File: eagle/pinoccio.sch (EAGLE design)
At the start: 59 parts, among them IC1 ATMEGA16U2QFN32, J1 AVR_SPI_PRG_6, Q1 16MHz, Q2 32.768k, Q3 16MHz, U1 MCP73831, U2 TPS78233, U4 ATMEGA128RFA1, X1 USB-MICROB, Y2 ANTENNA2SMD5

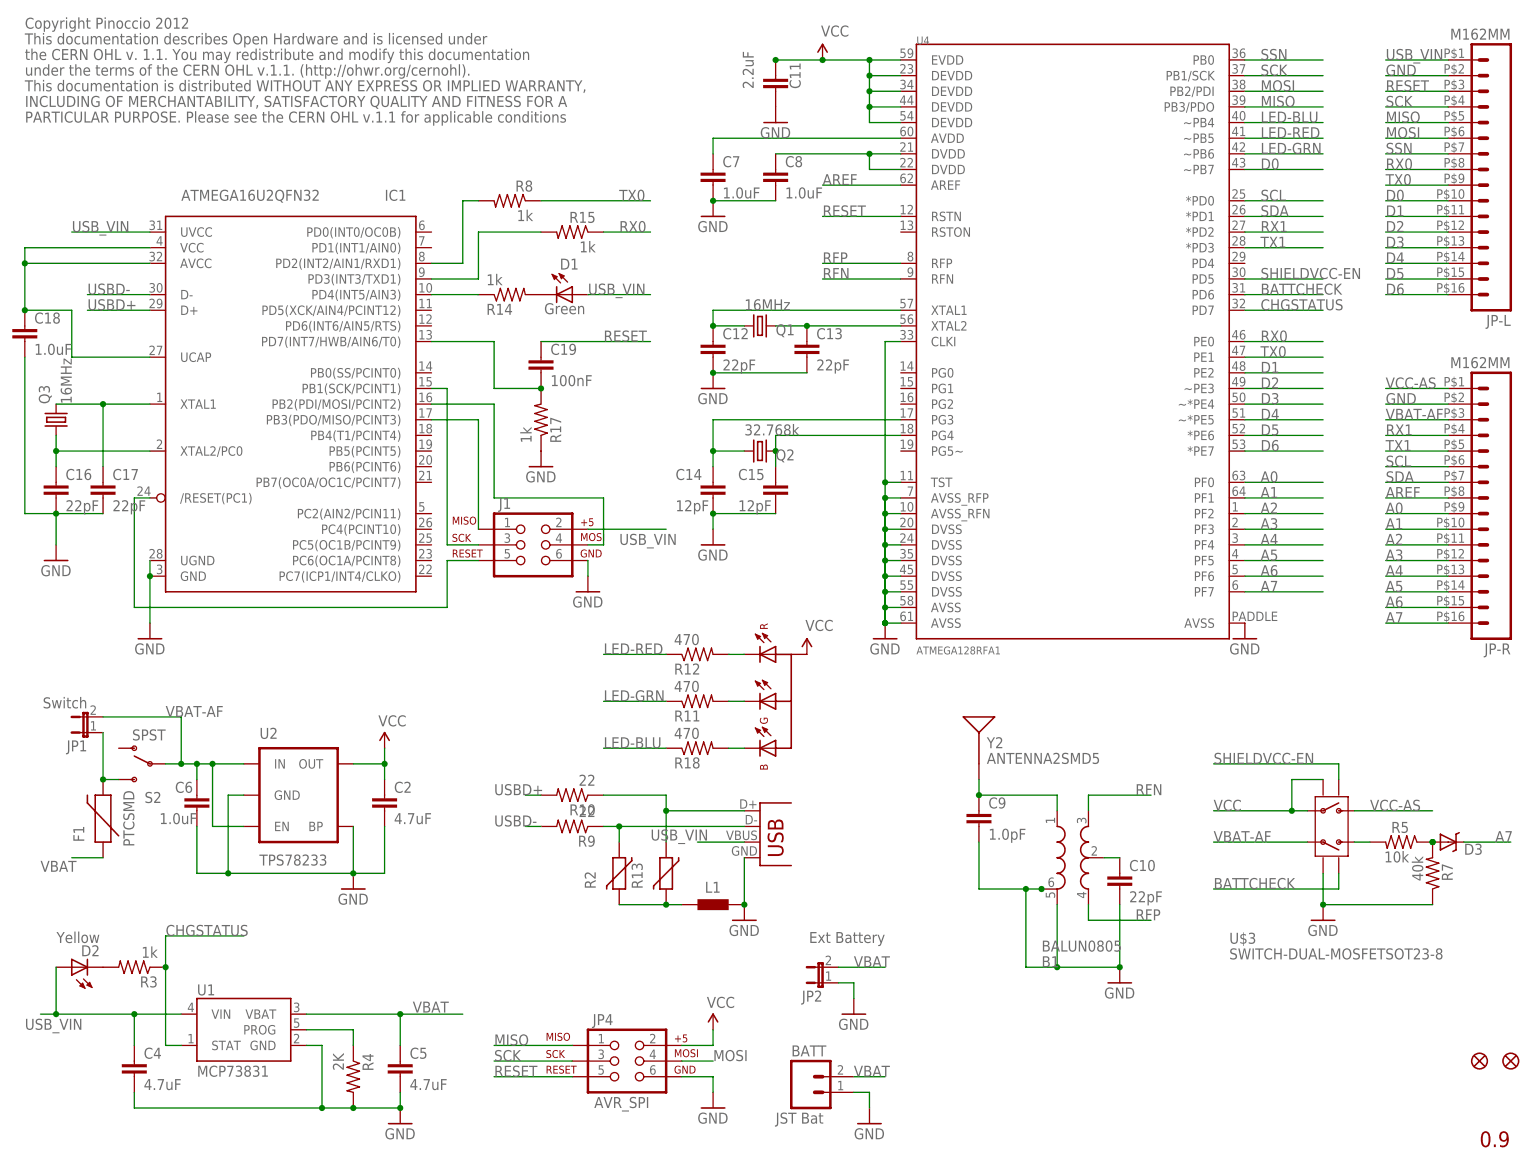
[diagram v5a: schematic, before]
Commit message: Fix changes needed for reset pullup resistor for 16U2
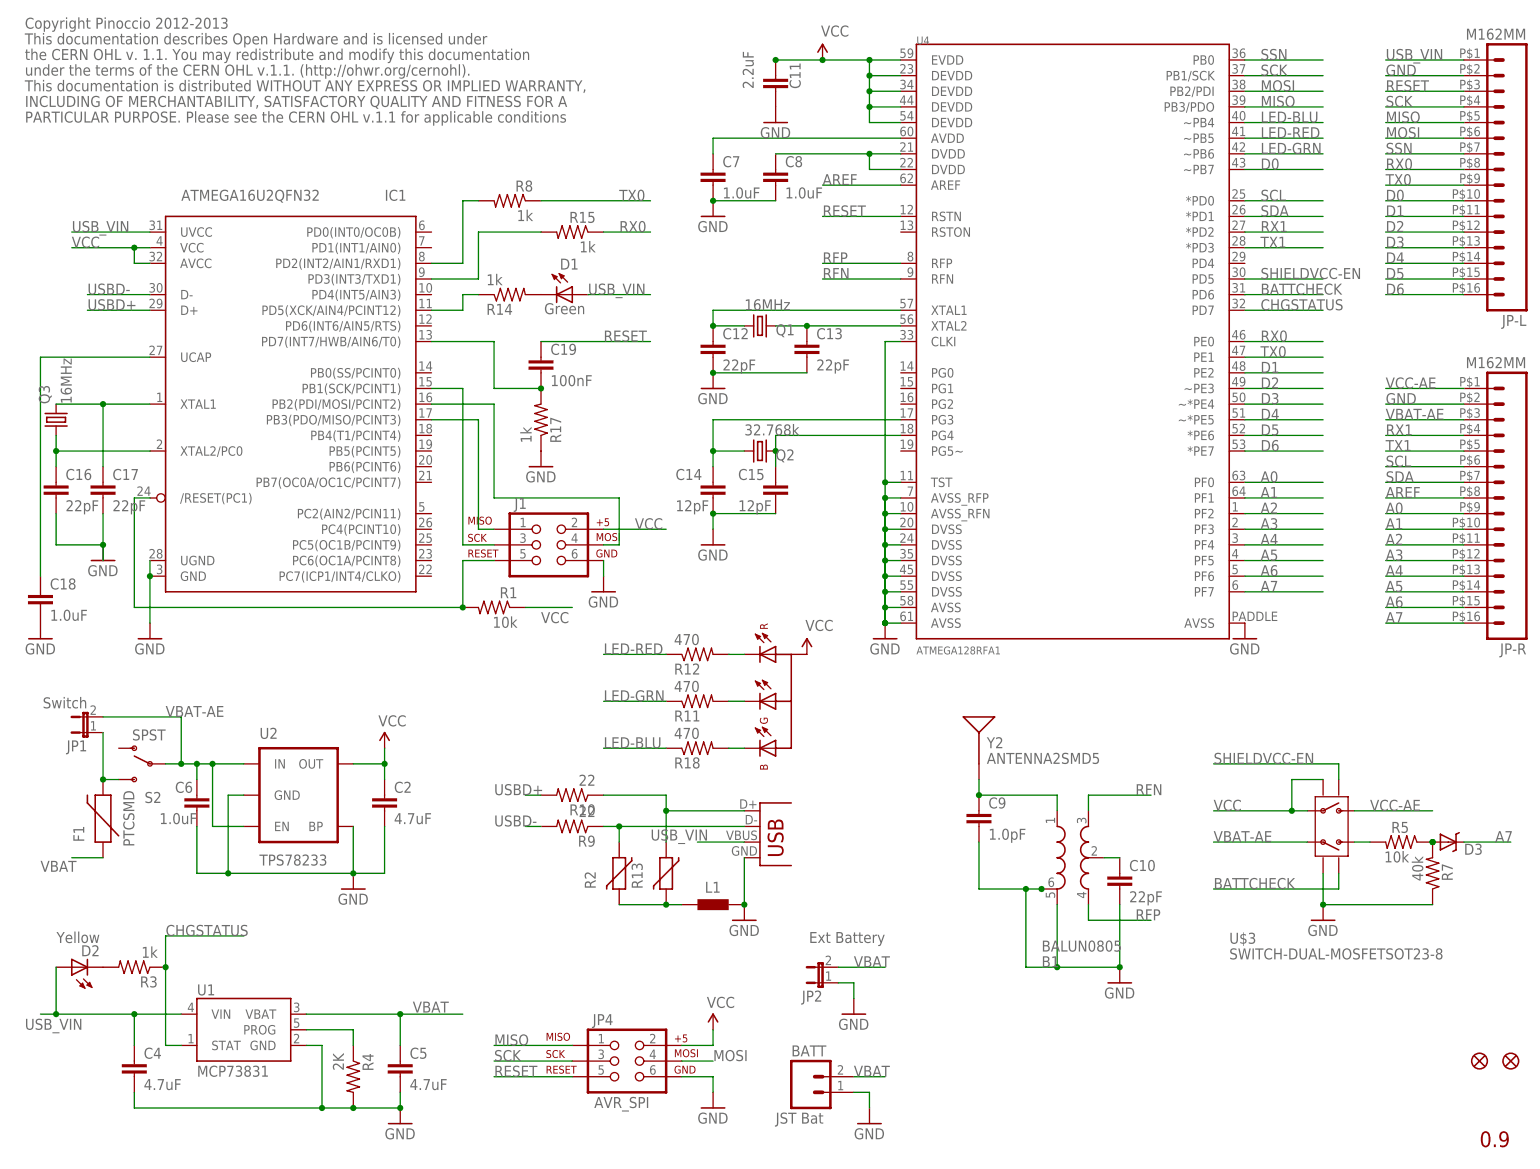
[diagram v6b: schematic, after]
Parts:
- added R1: 10k, Pinoccio:RESISTOR0402-RES
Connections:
- net VBAT-AF renamed VBAT-AE
- net VCC-AS renamed VCC-AE
- removed net N$23: C18.1, IC1.AVCC, IC1.UCAP, IC1.VCC
- removed net N$55: IC1./RESET(PC1), J1.5
- new net N$12: C18.1, IC1.UCAP
- new net N$7: IC1./RESET(PC1), J1.5, R1.2
- net N$59: now also IC1.PD5(XCK/AIN4/PCINT12); no longer IC1.PD4(INT5/AIN3)
- net USB_VIN: no longer J1.2
- net VCC: now also IC1.AVCC, IC1.VCC, J1.2, R1.1
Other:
- note added: "Copyright Pinoccio 2012-2013"
- note removed: "Copyright Pinoccio 2012"
- moved on the sheet: C18, J1, JP-L, JP-R

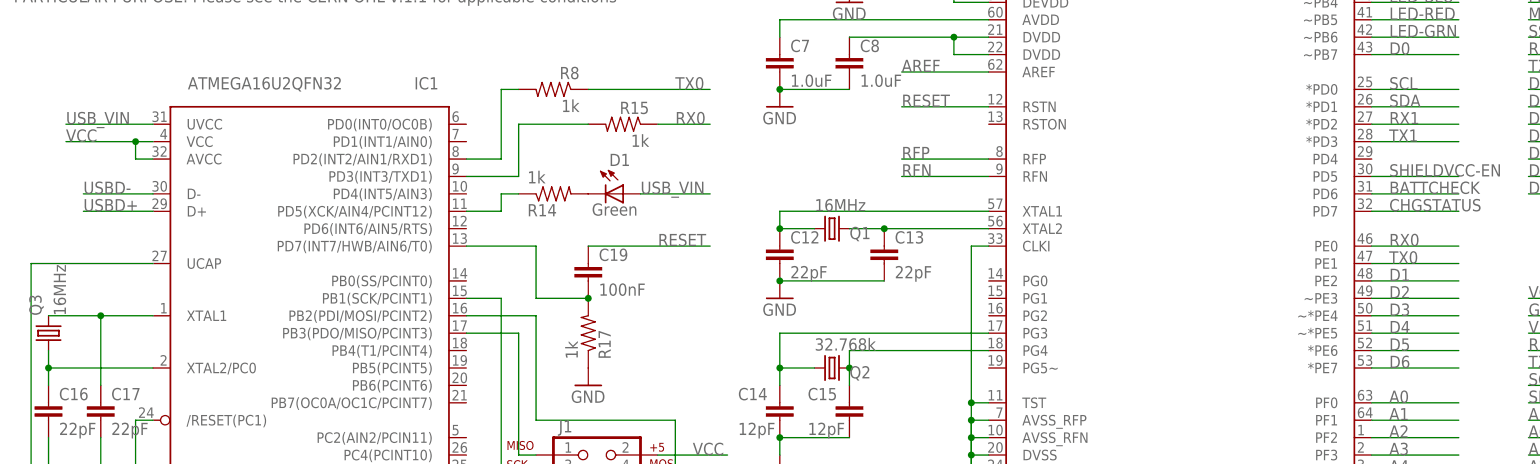
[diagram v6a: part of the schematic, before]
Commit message: re-cleaned up reset line to 16U2
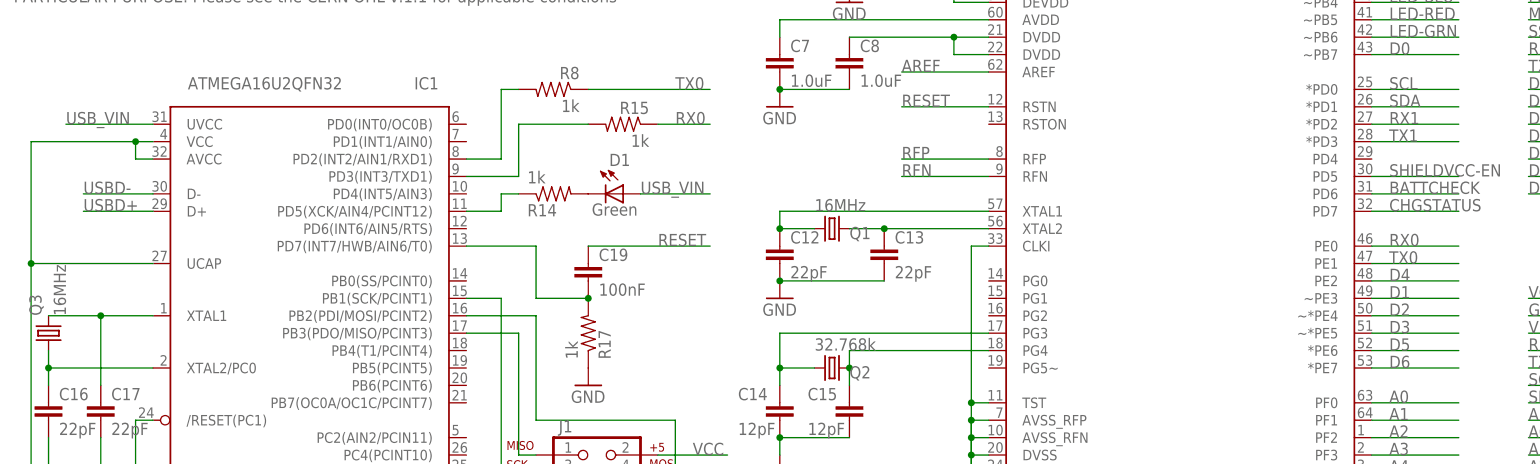
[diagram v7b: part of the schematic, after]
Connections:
- net D1: now also U4.~PE3; no longer U4.PE2
- net D2: now also U4.~*PE4; no longer U4.~PE3
- net D3: now also U4.~*PE5; no longer U4.~*PE4
- net D4: now also U4.PE2; no longer U4.~*PE5
- net N$12: now also IC1.AVCC, IC1.VCC
- net VCC: no longer IC1.AVCC, IC1.VCC
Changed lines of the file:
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@@
 <label x="101.6" y="101.6" size="1.778" layer="95"/>
-</segment>
-<segment>
-<pinref part="IC1" gate="G$1" pin="VCC"/>
-<wire x1="22.86" y1="147.32" x2="20.32" y2="147.32" width="0.1524" layer="91"/>
-<pinref part="IC1" gate="G$1" pin="AVCC"/>
-<wire x1="20.32" y1="147.32" x2="10.16" y2="147.32" width="0.1524" layer="91"/>
-<wire x1="22.86" y1="144.78" x2="20.32" y2="144.78" width="0.1524" layer="91"/>
-<wire x1="20.32" y1="144.78" x2="20.32" y2="147.32" width="0.1524" layer="91"/>
-<junction x="20.32" y="147.32"/>
-<label x="10.16" y="147.32" size="1.778" layer="95"/>
 </segment>
 </net>
@@
 </segment>
 <segment>
+<pinref part="U4" gate="G$1" pin="~PE3"/>
+<wire x1="200.66" y1="124.46" x2="213.36" y2="124.46" width="0.1524" layer="91"/>
+<label x="203.2" y="124.46" size="1.778" layer="95"/>
+</segment>
+</net>
+<net name="D2" class="0">
+<segment>
+<pinref part="JP-L" gate="G$1" pin="12"/>
+<wire x1="236.22" y1="149.86" x2="223.52" y2="149.86" width="0.1524" layer="91"/>
+<label x="223.52" y="149.86" size="1.778" layer="95"/>
+</segment>
+<segment>
+<pinref part="U4" gate="G$1" pin="~*PE4"/>
+<wire x1="200.66" y1="121.92" x2="213.36" y2="121.92" width="0.1524" layer="91"/>
+<label x="203.2" y="121.92" size="1.778" layer="95"/>
+</segment>
+</net>
+<net name="D3" class="0">
+<segment>
+<pinref part="JP-L" gate="G$1" pin="13"/>
+<wire x1="236.22" y1="147.32" x2="223.52" y2="147.32" width="0.1524" layer="91"/>
+<label x="223.52" y="147.32" size="1.778" layer="95"/>
+</segment>
+<segment>
+<pinref part="U4" gate="G$1" pin="~*PE5"/>
+<wire x1="200.66" y1="119.38" x2="213.36" y2="119.38" width="0.1524" layer="91"/>
+<label x="203.2" y="119.38" size="1.778" layer="95"/>
+</segment>
+</net>
+<net name="D4" class="0">
+<segment>
+<pinref part="JP-L" gate="G$1" pin="14"/>
+<wire x1="236.22" y1="144.78" x2="223.52" y2="144.78" width="0.1524" layer="91"/>
+<label x="223.52" y="144.78" size="1.778" layer="95"/>
+</segment>
+<segment>
 <pinref part="U4" gate="G$1" pin="PE2"/>
 <wire x1="200.66" y1="127" x2="213.36" y2="127" width="0.1524" layer="91"/>
 <label x="203.2" y="127" size="1.778" layer="95"/>
-</segment>
-</net>
-<net name="D2" class="0">
-<segment>
-<pinref part="JP-L" gate="G$1" pin="12"/>
-<wire x1="236.22" y1="149.86" x2="223.52" y2="149.86" width="0.1524" layer="91"/>
-<label x="223.52" y="149.86" size="1.778" layer="95"/>
-</segment>
-<segment>
-<pinref part="U4" gate="G$1" pin="~PE3"/>
-<wire x1="200.66" y1="124.46" x2="213.36" y2="124.46" width="0.1524" layer="91"/>
-<label x="203.2" y="124.46" size="1.778" layer="95"/>
-</segment>
-</net>
-<net name="D3" class="0">
-<segment>
-<pinref part="JP-L" gate="G$1" pin="13"/>
-<wire x1="236.22" y1="147.32" x2="223.52" y2="147.32" width="0.1524" layer="91"/>
-<label x="223.52" y="147.32" size="1.778" layer="95"/>
-</segment>
-<segment>
-<pinref part="U4" gate="G$1" pin="~*PE4"/>
-<wire x1="200.66" y1="121.92" x2="213.36" y2="121.92" width="0.1524" layer="91"/>
-<label x="203.2" y="121.92" size="1.778" layer="95"/>
-</segment>
-</net>
-<net name="D4" class="0">
-<segment>
-<pinref part="JP-L" gate="G$1" pin="14"/>
-<wire x1="236.22" y1="144.78" x2="223.52" y2="144.78" width="0.1524" layer="91"/>
-<label x="223.52" y="144.78" size="1.778" layer="95"/>
-</segment>
-<segment>
-<pinref part="U4" gate="G$1" pin="~*PE5"/>
-<wire x1="200.66" y1="119.38" x2="213.36" y2="119.38" width="0.1524" layer="91"/>
-<label x="203.2" y="119.38" size="1.778" layer="95"/>
 </segment>
 </net>
@@
 <wire x1="5.08" y1="93.98" x2="5.08" y2="129.54" width="0.1524" layer="91"/>
 <wire x1="5.08" y1="129.54" x2="22.86" y2="129.54" width="0.1524" layer="91"/>
-</segment>
-</net>
+<pinref part="IC1" gate="G$1" pin="VCC"/>
+<wire x1="22.86" y1="147.32" x2="20.32" y2="147.32" width="0.1524" layer="91"/>
+<wire x1="20.32" y1="147.32" x2="5.08" y2="147.32" width="0.1524" layer="91"/>
+<wire x1="5.08" y1="147.32" x2="5.08" y2="129.54" width="0.1524" layer="91"/>
+<pinref part="IC1" gate="G$1" pin="AVCC"/>
+<wire x1="22.86" y1="144.78" x2="20.32" y2="144.78" width="0.1524" layer="91"/>
+<wire x1="20.32" y1="144.78" x2="20.32" y2="147.32" width="0.1524" layer="91"/>
+<junction x="20.32" y="147.32"/>
+<junction x="5.08" y="129.54"/>
+</segment>
+</net>

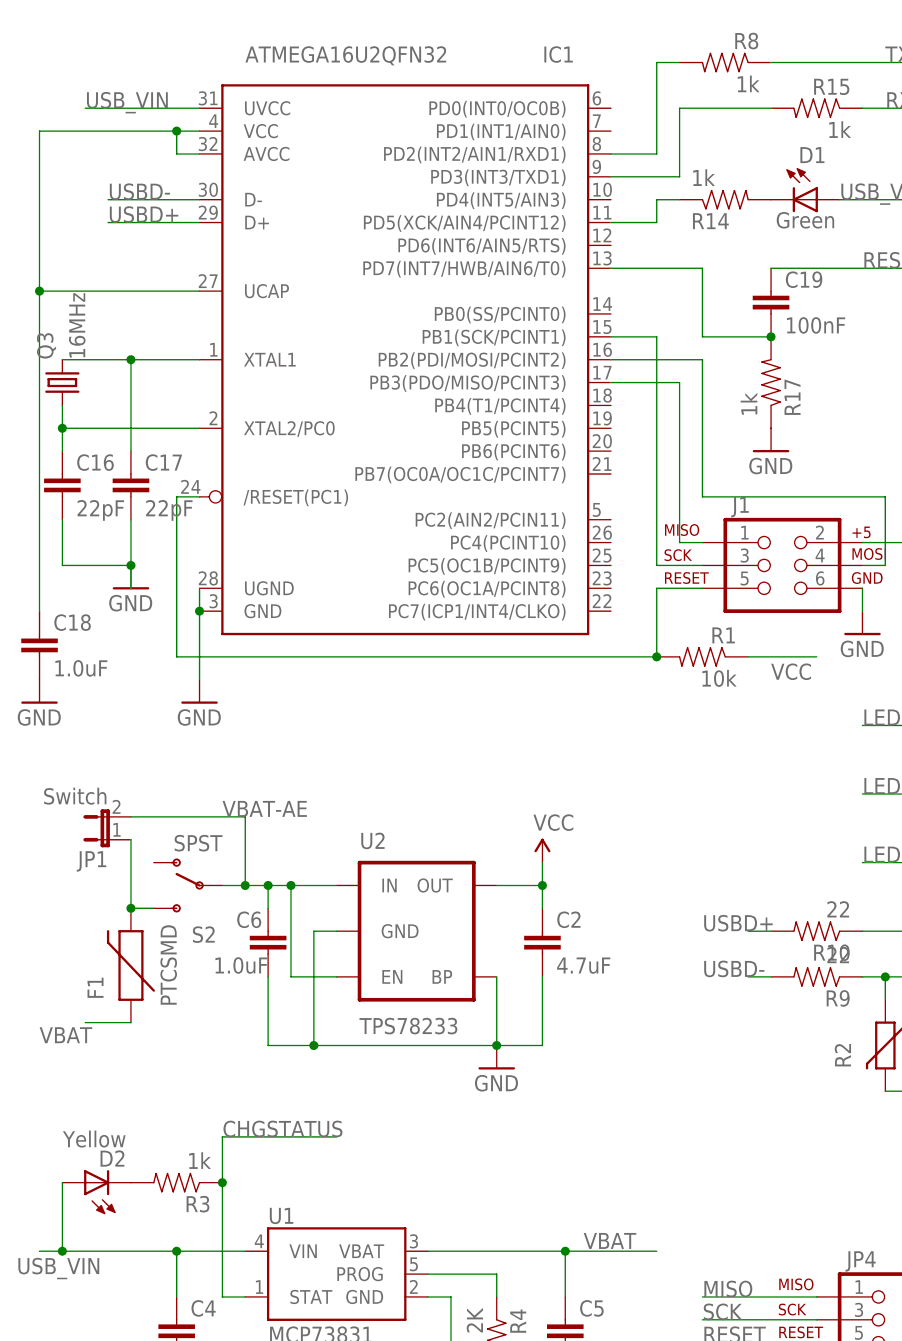
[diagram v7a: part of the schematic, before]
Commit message: Added new socker header datasheet
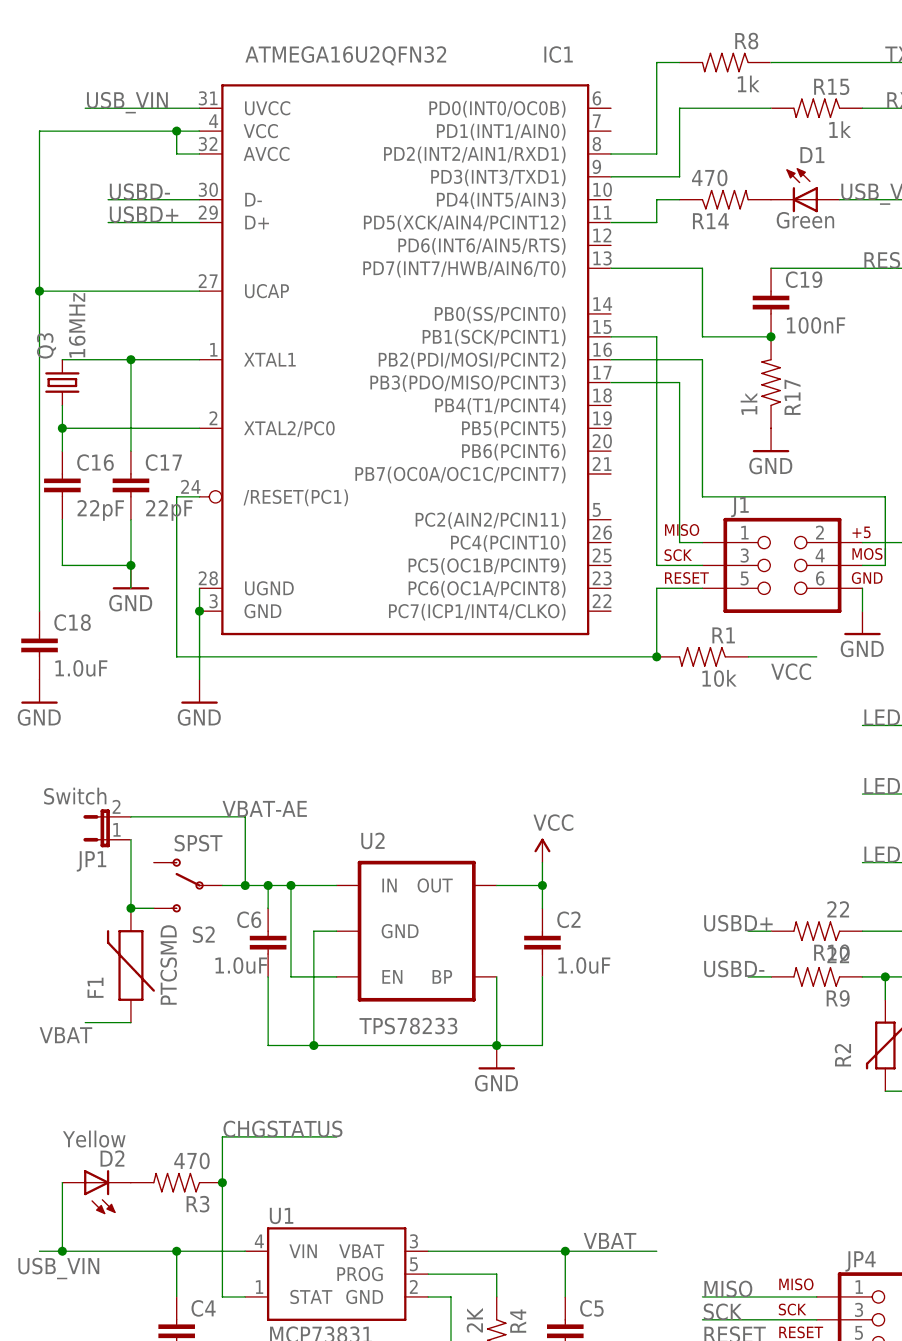
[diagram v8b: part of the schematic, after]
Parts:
- C2: value 4.7uF -> 1.0uF
- R14, R3: value 1k -> 470
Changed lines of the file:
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@@
 <parts>
 <part name="FRAME1" library="Pinoccio" deviceset="FRAME-LETTER" device=""/>
-<part name="C2" library="Pinoccio" deviceset="CAP" device="0402-CAP" value="4.7uF"/>
+<part name="C2" library="Pinoccio" deviceset="CAP" device="0402-CAP" value="1.0uF"/>
 <part name="JP4" library="Pinoccio" deviceset="AVR_SPI_PRG_6" device="" value="AVR_SPI"/>
 <part name="P+1" library="SparkFun" deviceset="VCC" device=""/>
@@
 <part name="GND20" library="supply1" deviceset="GND" device=""/>
 <part name="D2" library="Pinoccio" deviceset="LED" device="0603" value="Yellow"/>
-<part name="R3" library="Pinoccio" deviceset="RESISTOR" device="0402-RES" value="1k"/>
+<part name="R3" library="Pinoccio" deviceset="RESISTOR" device="0402-RES" value="470"/>
 <part name="X1" library="Pinoccio" deviceset="USB" device="-MICROB"/>
 <part name="GND21" library="supply1" deviceset="GND" device=""/>
@@
 <part name="J1" library="Pinoccio" deviceset="AVR_SPI_PRG_6" device=""/>
 <part name="D1" library="Pinoccio" deviceset="LED" device="0603" value="Green"/>
-<part name="R14" library="Pinoccio" deviceset="RESISTOR" device="0402-RES" value="1k"/>
+<part name="R14" library="Pinoccio" deviceset="RESISTOR" device="0402-RES" value="470"/>
 <part name="GND5" library="SparkFun" deviceset="GND" device=""/>
 <part name="P+2" library="SparkFun" deviceset="VCC" device=""/>
